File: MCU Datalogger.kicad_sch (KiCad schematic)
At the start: 25 parts, among them U1 24LC1025, U2 24LC1025, U3 DS1337S_, U4 ATMEGA328P-AU, Y1 32.768KHz, Y2 16MHz

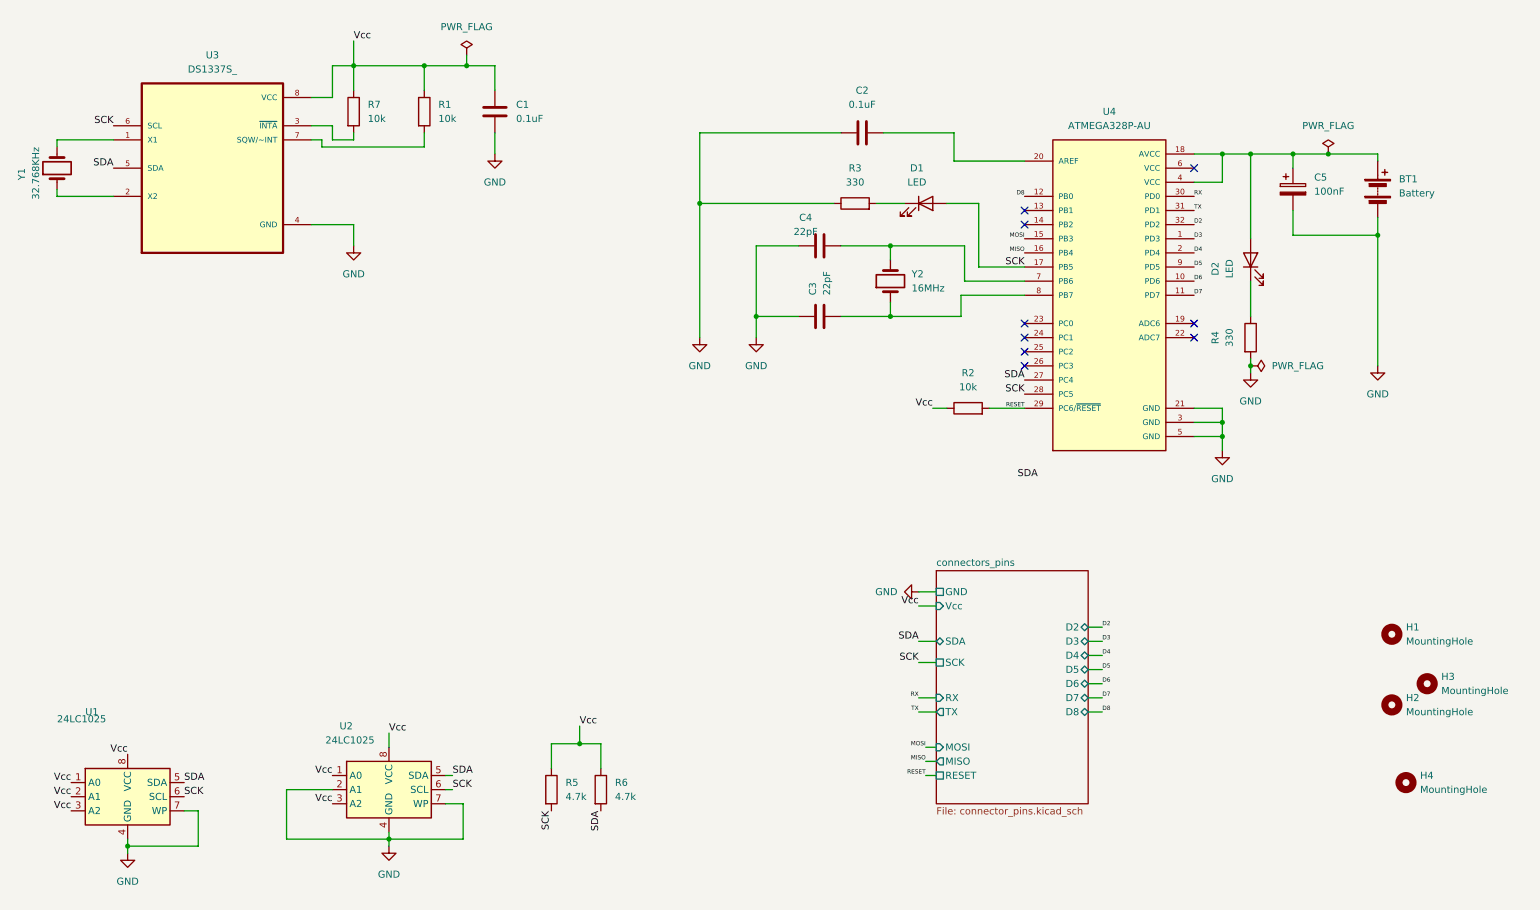
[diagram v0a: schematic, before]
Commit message: complete layout of components
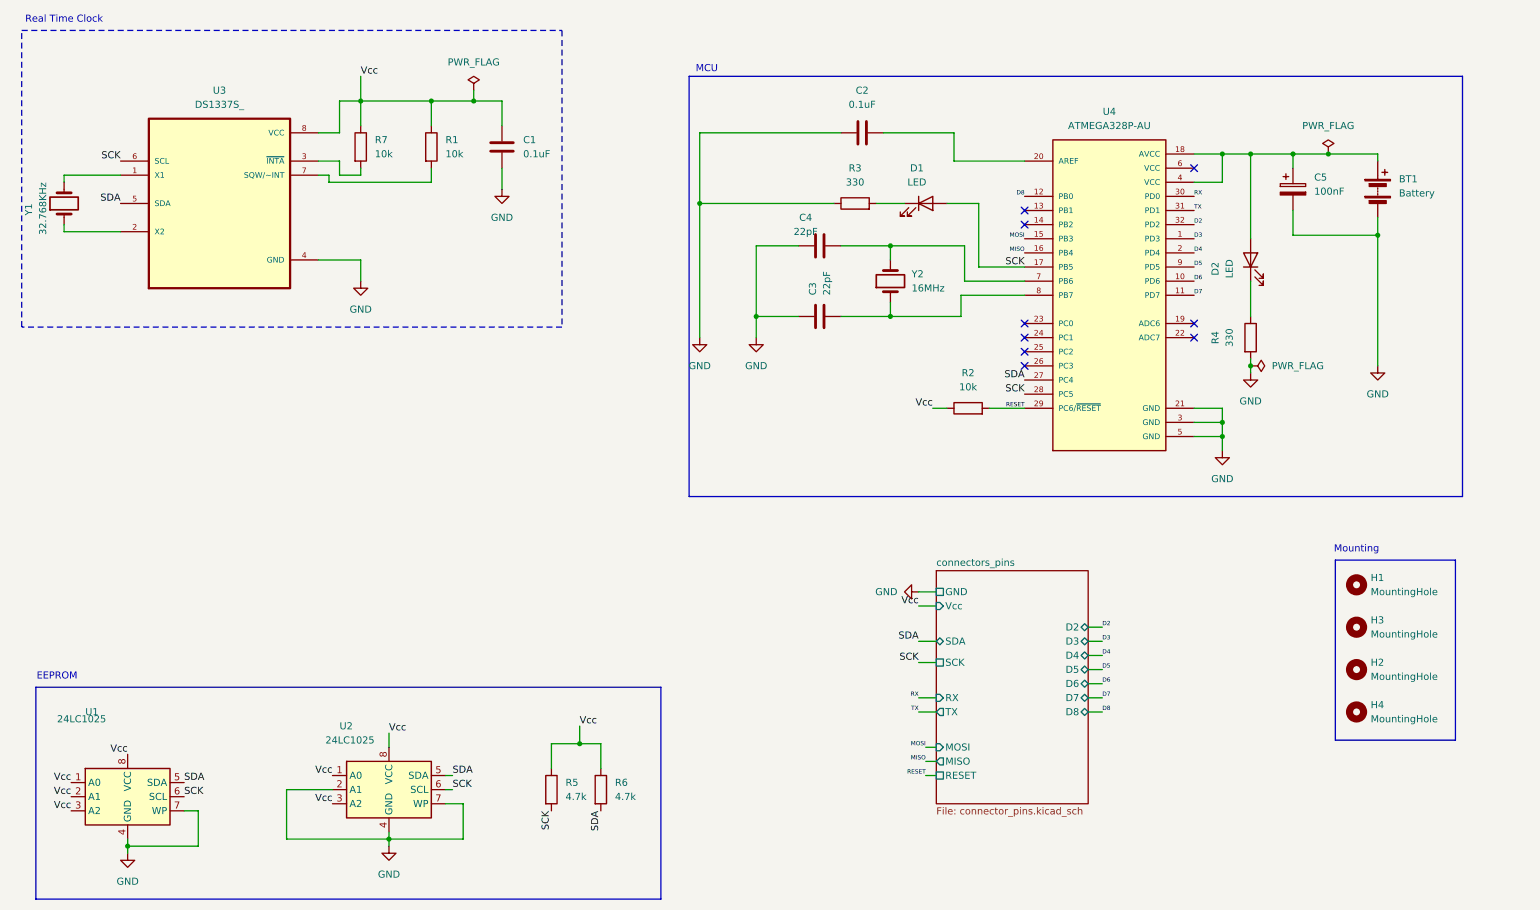
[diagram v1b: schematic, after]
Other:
- note added: "EEPROM"
- note added: "MCU"
- note added: "Mounting"
- note added: "Real Time Clock"
- moved on the sheet: C1, H1, H2, H3, H4, R1, R7, U3, Y1
